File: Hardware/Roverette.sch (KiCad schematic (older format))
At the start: 40 parts, among them SW1 SW_Push, U1 ESP32-WROOM-32U

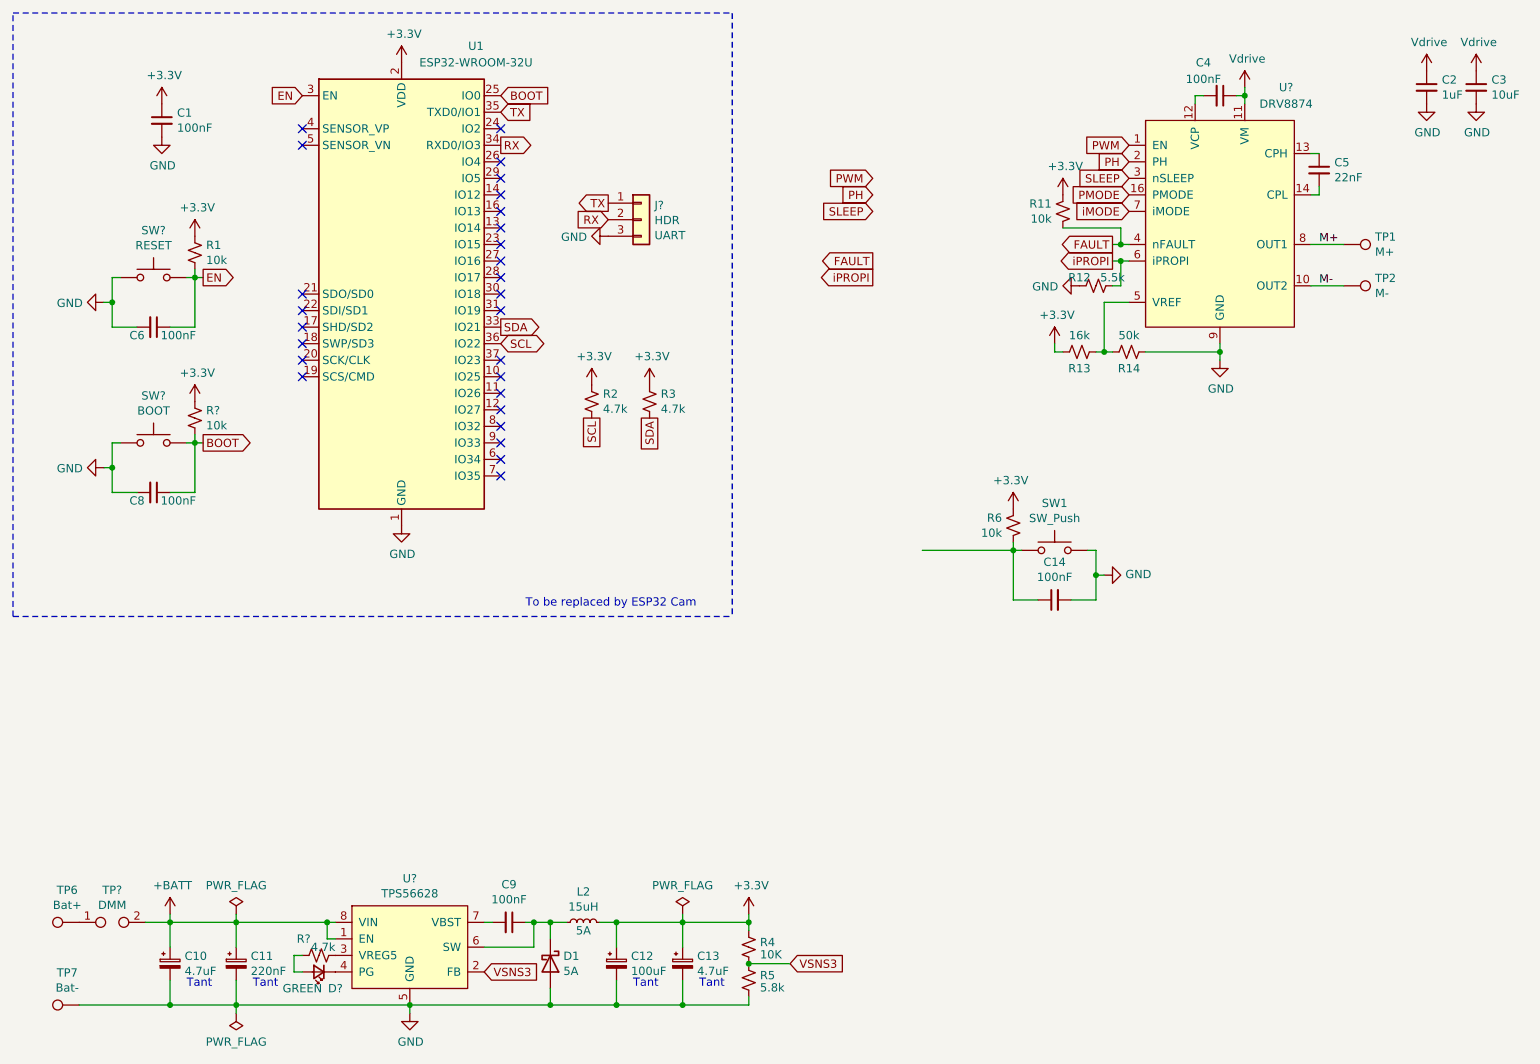
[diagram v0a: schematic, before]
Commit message: Schematic divided into sub-sheets
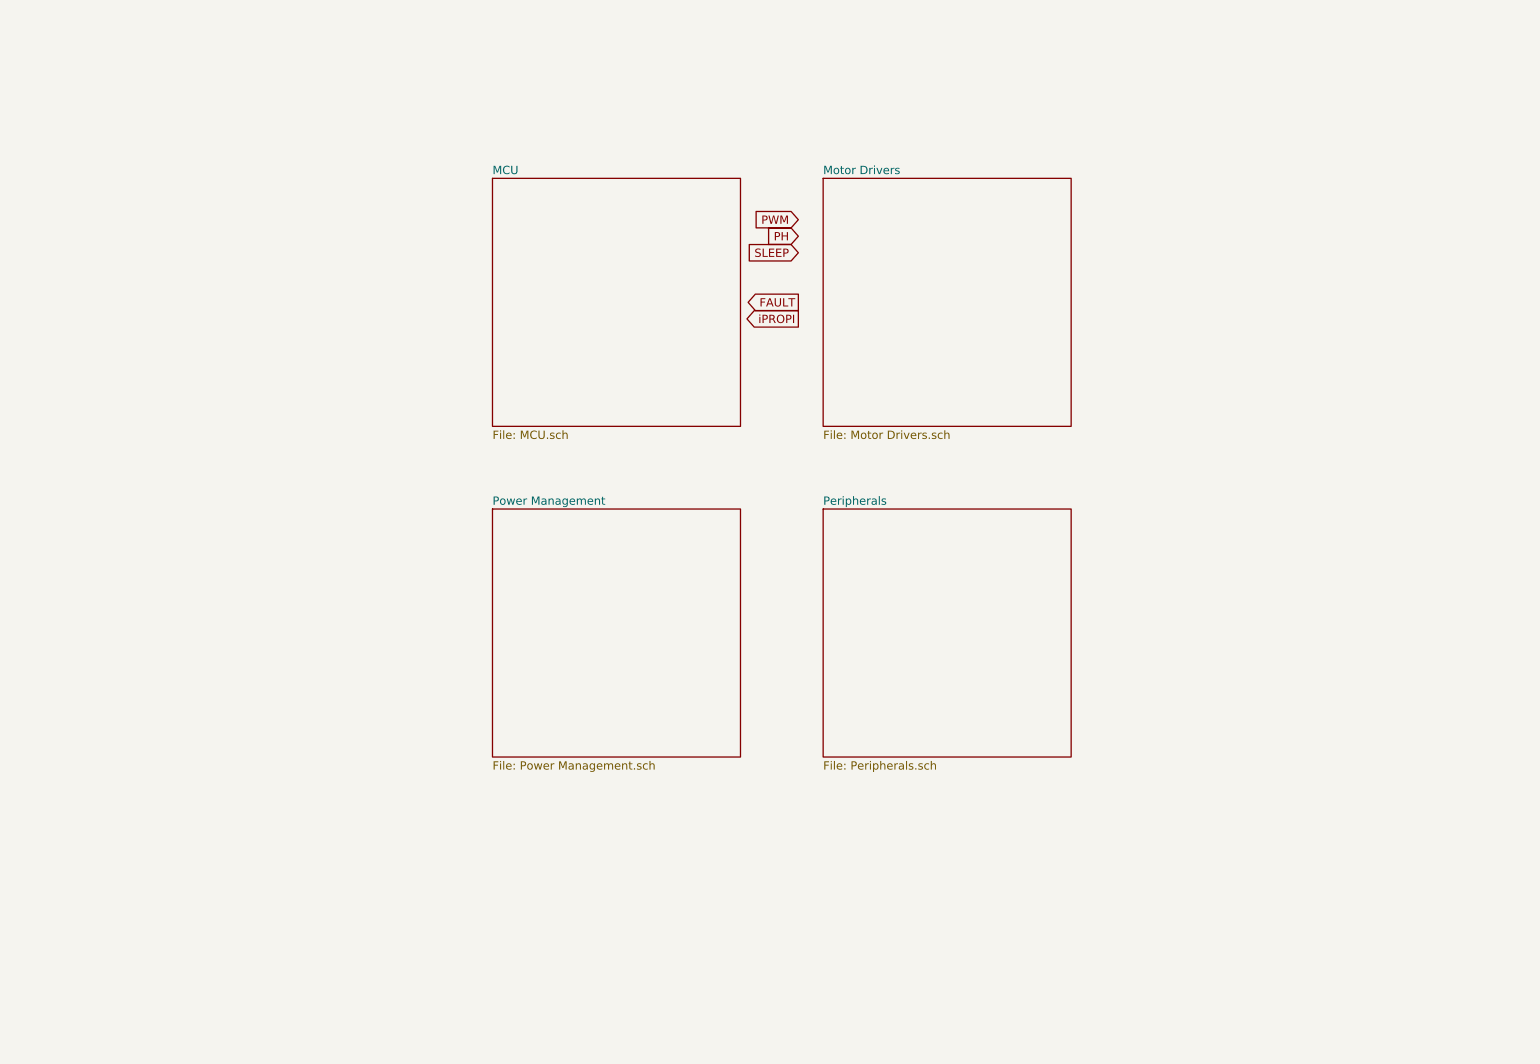
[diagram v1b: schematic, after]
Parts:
- removed C1, C14, C6, C8, C9: 100nF, Capacitor_SMD:C_0805_2012Metric, symbol Device:C_Small
- removed C10, C13: 4.7uF, Capacitor_Tantalum_SMD:CP_EIA-3528-15_AVX-H, symbol Device:CP_Small
- removed C11: 220nF, Capacitor_Tantalum_SMD:CP_EIA-3216-18_Kemet-A, symbol Device:CP_Small
- removed C12: 100uF, Capacitor_Tantalum_SMD:CP_EIA-7343-31_Kemet-D, symbol Device:CP_Small
- removed C2: 1uF, Resistor_SMD:R_0603_1608Metric, symbol Device:C_Small
- removed C3: 10uF, Capacitor_SMD:C_2220_5650Metric, symbol Device:C_Small
- removed C4: 100nF, Resistor_SMD:R_0603_1608Metric, symbol Device:C_Small
- removed C5: 22nF, Resistor_SMD:R_0603_1608Metric, symbol Device:C_Small
- removed D1: 5A, Diode_SMD:D_SOD-123F, symbol Device:D_Schottky
- removed D?: GREEN, symbol Device:LED_Small
- removed J?: HDR, symbol Connector_Generic:Conn_01x03
- removed L2: 15uH, Inductor_SMD:L_Neosid_SMs42, symbol Device:L_Small
- removed R1, R6, R?: 10k, Resistor_SMD:R_0805_2012Metric, symbol Device:R_Small_US
- removed R11: 10k, Resistor_SMD:R_0603_1608Metric, symbol Device:R_Small_US
- removed R12: 5.5k, Resistor_SMD:R_0603_1608Metric, symbol Device:R_Small_US
- removed R13: 16k, Resistor_SMD:R_0603_1608Metric, symbol Device:R_Small_US
- removed R14: 50k, Resistor_SMD:R_0603_1608Metric, symbol Device:R_Small_US
- removed R2, R3: 4.7k, Resistor_SMD:R_0603_1608Metric, symbol Device:R_Small_US
- removed R4: 10K, Resistor_SMD:R_0805_2012Metric, symbol Device:R_Small_US
- removed R5: 5.8k, Resistor_SMD:R_0805_2012Metric, symbol Device:R_Small_US
- removed R?: 4.7k, Resistor_SMD:R_0805_2012Metric, symbol Device:R_Small_US
- removed SW1, SW? (x2): SW_Push, Button_Switch_SMD:SW_SPST_CK_RS282G05A3, symbol Switch:SW_Push
- removed TP1: M+, TestPoint:TestPoint_Keystone_5000-5004_Miniature, symbol Connector:TestPoint
- removed TP2: M-, TestPoint:TestPoint_Keystone_5000-5004_Miniature, symbol Connector:TestPoint
- removed TP6: Bat+, TestPoint:TestPoint_Keystone_5000-5004_Miniature, symbol Connector:TestPoint
- removed TP7: Bat-, TestPoint:TestPoint_Keystone_5000-5004_Miniature, symbol Connector:TestPoint
- removed TP?: TestPoint_2Pole, TestPoint:TestPoint_2Pads_Pitch2.54mm_Drill0.8mm, symbol Connector:TestPoint_2Pole
- removed U1: ESP32-WROOM-32U, RF_Module:ESP32-WROOM-32U, symbol RF_Module:ESP32-WROOM-32U
- removed U?: DRV8874, Package_SO:HTSSOP-16-1EP_4.4x5mm_P0.65mm_EP3.4x5mm_Mask3x3mm_ThermalVias, symbol Driver_Motor:DRV8874
- removed U?: TPS56628, Package_SO:HSOP-8-1EP_3.9x4.9mm_P1.27mm_EP2.41x3.1mm_ThermalVias, symbol Power_Management:TPS56628
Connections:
- no-connect marks 27 -> 0
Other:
- note removed: "Tant"
- note removed: "To be replaced by ESP32 Cam"

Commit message: Motor driver and power management subsheet converted to blocks
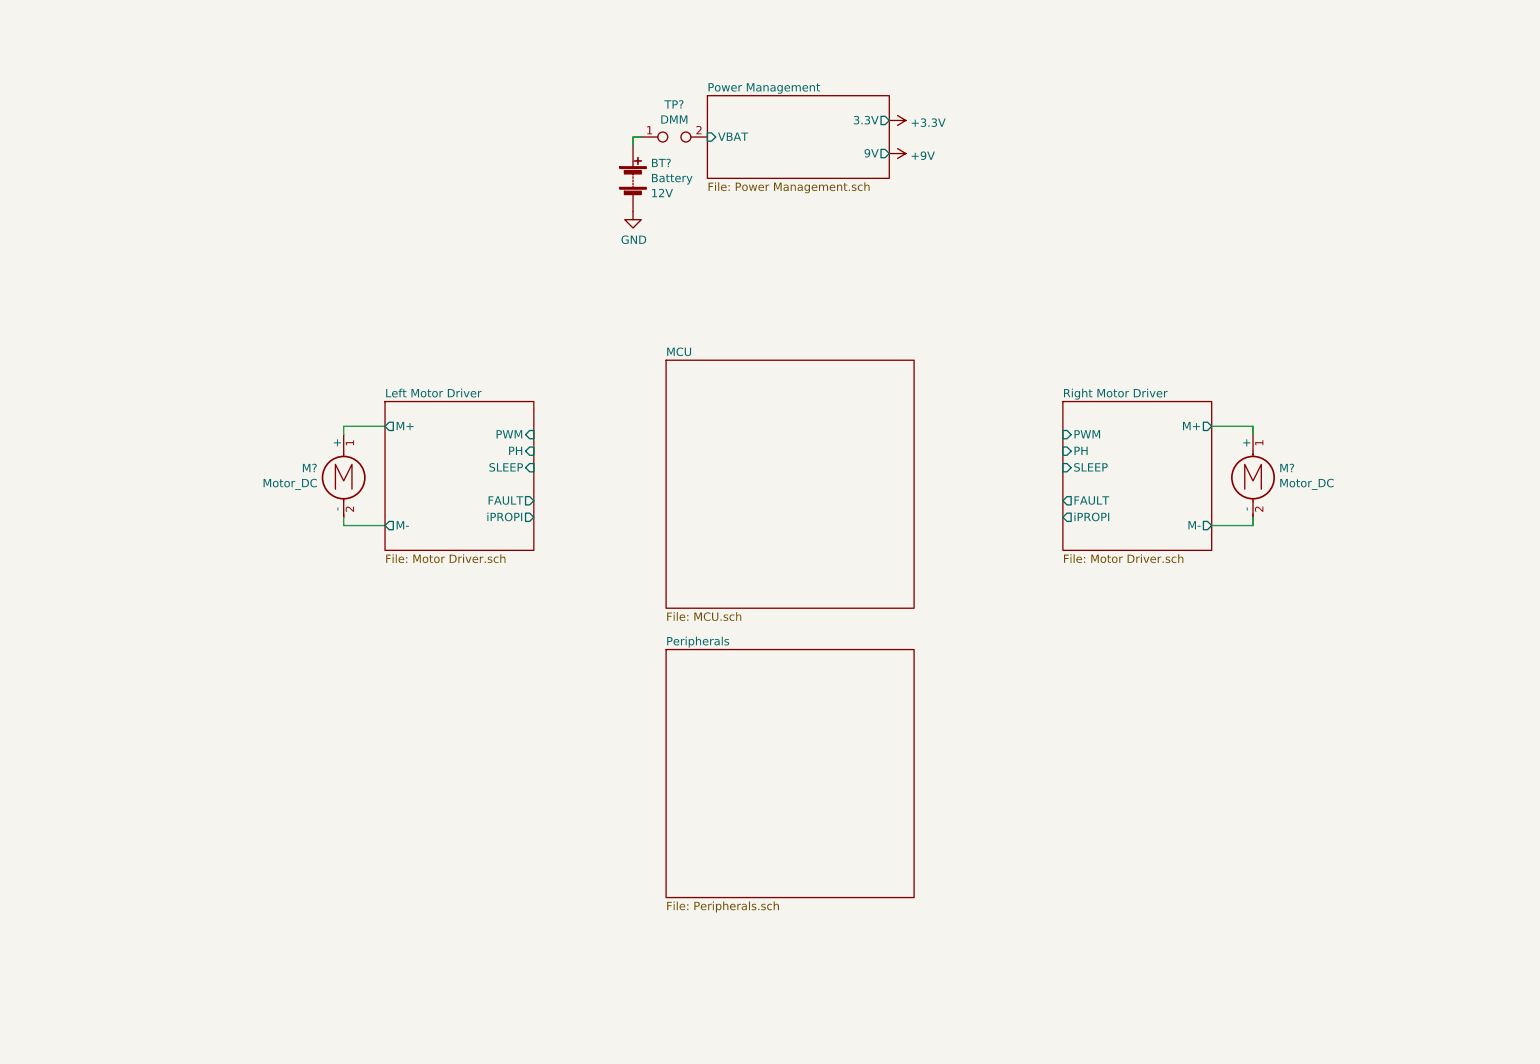
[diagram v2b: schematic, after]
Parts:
- added BT?: Battery, symbol Device:Battery
- added M? (x2): Motor_DC, symbol Motor:Motor_DC
- added TP?: TestPoint_2Pole, TestPoint:TestPoint_2Pads_Pitch2.54mm_Drill0.8mm, symbol Connector:TestPoint_2Pole
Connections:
- new net: BT?.1 (+), TP?.1
- new net GND: BT?.2 (-)
- new net Left Motor Driver/M+: M?.1 (+)
- new net Left Motor Driver/M-: M?.2 (-)
- new net Power Management/VBAT: TP?.2
- new net Right Motor Driver/M+: M?.1 (+)
- new net Right Motor Driver/M-: M?.2 (-)
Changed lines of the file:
@@
 $Descr A4 11693 8268
 encoding utf-8
-Sheet 1 5
+Sheet 1 6
 Title "Roverette"
 Date "2020-10-11"
@@
 Comment4 ""
 $EndDescr
-Text GLabel 5850 2250 0    50   Input ~ 0
-PWM
-Text GLabel 5850 2350 0    50   Input ~ 0
-PH
-Text GLabel 5850 2450 0    50   Input ~ 0
-SLEEP
-Text GLabel 5850 2750 0    50   Output ~ 0
-FAULT
-Text GLabel 5850 2850 0    50   Output ~ 0
-iPROPI
 $Sheet
-S 4000 2000 1500 1500
+S 5050 3100 1500 1500
 U 5FEFFC20
 F0 "MCU" 50
@@
 $EndSheet
 $Sheet
-S 6000 2000 1500 1500
-U 5FF00151
-F0 "Motor Drivers" 50
-F1 "Motor Drivers.sch" 50
-$EndSheet
-$Sheet
-S 4000 4000 1500 1500
+S 5300 1500 1100 500
 U 5FF0069C
 F0 "Power Management" 50
 F1 "Power Management.sch" 50
+F2 "VBAT" I L 5300 1750 50
+F3 "3.3V" O R 6400 1650 50
+F4 "9V" O R 6400 1850 50
 $EndSheet
 $Sheet
-S 6000 4000 1500 1500
+S 5050 4850 1500 1500
 U 5FF00BCF
 F0 "Peripherals" 50
 F1 "Peripherals.sch" 50
 $EndSheet
+$Sheet
+S 3350 3350 900  900
+U 5FF00151
+F0 "Left Motor Driver" 50
+F1 "Motor Driver.sch" 50
+F2 "M-" O L 3350 4100 50
+F3 "PWM" I R 4250 3550 50
+F4 "PH" I R 4250 3650 50
+F5 "SLEEP" I R 4250 3750 50
+F6 "FAULT" O R 4250 3950 50
+F7 "iPROPI" O R 4250 4050 50
+F8 "M+" O L 3350 3500 50
+$EndSheet
+$Comp
+L Motor:Motor_DC M?
+U 1 1 5FF290D9
+P 3100 3750
+F 0 "M?" H 3258 3746 50  0000 L CNN
+F 1 "Motor_DC" H 3258 3655 50  0000 L CNN
+F 2 "" H 3100 3660 50  0001 C CNN
+F 3 "~" H 3100 3660 50  0001 C CNN
+	1    3100 3750
+	-1   0    0    -1
+$EndComp
+Wire Wire Line
+	3350 3500 3100 3500
+Wire Wire Line
+	3100 3500 3100 3550
+Wire Wire Line
+	3350 4100 3100 4100
+Wire Wire Line
+	3100 4100 3100 4050
+$Sheet
+S 7450 3350 900  900
+U 5FF2CF13
+F0 "Right Motor Driver" 50
+F1 "Motor Driver.sch" 50
+F2 "M-" O R 8350 4100 50
+F3 "PWM" I L 7450 3550 50
+F4 "PH" I L 7450 3650 50
+F5 "SLEEP" I L 7450 3750 50
+F6 "FAULT" O L 7450 3950 50
+F7 "iPROPI" O L 7450 4050 50
+F8 "M+" O R 8350 3500 50
+$EndSheet
+Wire Wire Line
+	8600 4100 8600 4050
+Wire Wire Line
+	8350 4100 8600 4100
+Wire Wire Line
+	8600 3500 8600 3550
+Wire Wire Line
+	8350 3500 8600 3500
+$Comp
+L Motor:Motor_DC M?
+U 1 1 5FF2CF19
+P 8600 3750
+F 0 "M?" H 8758 3746 50  0000 L CNN
+F 1 "Motor_DC" H 8758 3655 50  0000 L CNN
+F 2 "" H 8600 3660 50  0001 C CNN
+F 3 "~" H 8600 3660 50  0001 C CNN
+	1    8600 3750
+	1    0    0    -1
+$EndComp
+$Comp
+L power:+3.3V #PWR?
+U 1 1 5FF308D0
+P 6400 1650
+F 0 "#PWR?" H 6400 1500 50  0001 C CNN
+F 1 "+3.3V" V 6415 1778 50  0000 L CNN
+F 2 "" H 6400 1650 50  0001 C CNN
+F 3 "" H 6400 1650 50  0001 C CNN
+	1    6400 1650
+	0    1    1    0
+$EndComp
+$Comp
+L power:+9V #PWR?
+U 1 1 5FF30D7D
+P 6400 1850
+F 0 "#PWR?" H 6400 1700 50  0001 C CNN
+F 1 "+9V" V 6415 1978 50  0000 L CNN
+F 2 "" H 6400 1850 50  0001 C CNN
+F 3 "" H 6400 1850 50  0001 C CNN
+	1    6400 1850
+	0    1    1    0
+$EndComp
+$Comp
+L Device:Battery BT?
+U 1 1 5FF30336
+P 4850 2000
+F 0 "BT?" H 4958 2091 50  0000 L CNN
+F 1 "Battery" H 4958 2000 50  0000 L CNN
+F 2 "" V 4850 2060 50  0001 C CNN
+F 3 "~" V 4850 2060 50  0001 C CNN
+F 4 "12V" H 4958 1909 50  0000 L CNN "Field4"
+	1    4850 2000
+	1    0    0    -1
+$EndComp
+$Comp
+L power:GND #PWR?
+U 1 1 5FF31DAB
+P 4850 2200
+F 0 "#PWR?" H 4850 1950 50  0001 C CNN
+F 1 "GND" H 4855 2027 50  0000 C CNN
+F 2 "" H 4850 2200 50  0001 C CNN
+F 3 "" H 4850 2200 50  0001 C CNN
+	1    4850 2200
+	1    0    0    -1
+$EndComp
+$Comp
+L Connector:TestPoint_2Pole TP?
+U 1 1 5FF3E3D0
+P 5100 1750
+AR Path="/5FF3E3D0" Ref="TP?"  Part="1"
+AR Path="/5FF0069C/5FF3E3D0" Ref="TP?"  Part="1"
+F 0 "TP?" H 5100 1945 50  0000 C CNN
+F 1 "TestPoint_2Pole" H 5100 1854 50  0001 C CNN
+F 2 "TestPoint:TestPoint_2Pads_Pitch2.54mm_Drill0.8mm" H 5100 1750 50  0001 C CNN
+F 3 "~" H 5100 1750 50  0001 C CNN
+F 4 "DMM" H 5100 1854 50  0000 C CNN "Field4"
+	1    5100 1750
+	1    0    0    -1
+$EndComp
+Wire Wire Line
+	4900 1750 4850 1750
+Wire Wire Line
+	4850 1750 4850 1800
 $EndSCHEMATC

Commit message: Readme updated
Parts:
- gave numbers to parts that had none: 4
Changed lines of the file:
@@
 $EndSheet
 $Comp
-L Motor:Motor_DC M?
+L Motor:Motor_DC M1
 U 1 1 5FF290D9
 P 3100 3750
-F 0 "M?" H 3258 3746 50  0000 L CNN
+F 0 "M1" H 3258 3746 50  0000 L CNN
 F 1 "Motor_DC" H 3258 3655 50  0000 L CNN
 F 2 "" H 3100 3660 50  0001 C CNN
@@
 	8350 3500 8600 3500
 $Comp
-L Motor:Motor_DC M?
+L Motor:Motor_DC M2
 U 1 1 5FF2CF19
 P 8600 3750
-F 0 "M?" H 8758 3746 50  0000 L CNN
+F 0 "M2" H 8758 3746 50  0000 L CNN
 F 1 "Motor_DC" H 8758 3655 50  0000 L CNN
 F 2 "" H 8600 3660 50  0001 C CNN
@@
 $EndComp
 $Comp
-L power:+3.3V #PWR?
+L power:+3.3V #PWR01
 U 1 1 5FF308D0
 P 6400 1650
-F 0 "#PWR?" H 6400 1500 50  0001 C CNN
+F 0 "#PWR01" H 6400 1500 50  0001 C CNN
 F 1 "+3.3V" V 6415 1778 50  0000 L CNN
 F 2 "" H 6400 1650 50  0001 C CNN
@@
 $EndComp
 $Comp
-L power:+9V #PWR?
+L power:+9V #PWR02
 U 1 1 5FF30D7D
 P 6400 1850
-F 0 "#PWR?" H 6400 1700 50  0001 C CNN
+F 0 "#PWR02" H 6400 1700 50  0001 C CNN
 F 1 "+9V" V 6415 1978 50  0000 L CNN
 F 2 "" H 6400 1850 50  0001 C CNN
@@
 $EndComp
 $Comp
-L Device:Battery BT?
+L Device:Battery BT1
 U 1 1 5FF30336
 P 4850 2000
-F 0 "BT?" H 4958 2091 50  0000 L CNN
+F 0 "BT1" H 4958 2091 50  0000 L CNN
 F 1 "Battery" H 4958 2000 50  0000 L CNN
 F 2 "" V 4850 2060 50  0001 C CNN
@@
 $EndComp
 $Comp
-L power:GND #PWR?
+L power:GND #PWR03
 U 1 1 5FF31DAB
 P 4850 2200
-F 0 "#PWR?" H 4850 1950 50  0001 C CNN
+F 0 "#PWR03" H 4850 1950 50  0001 C CNN
 F 1 "GND" H 4855 2027 50  0000 C CNN
 F 2 "" H 4850 2200 50  0001 C CNN
@@
 $EndComp
 $Comp
-L Connector:TestPoint_2Pole TP?
+L Connector:TestPoint_2Pole TP1
 U 1 1 5FF3E3D0
 P 5100 1750
-AR Path="/5FF3E3D0" Ref="TP?"  Part="1"
+AR Path="/5FF3E3D0" Ref="TP1"  Part="1"
 AR Path="/5FF0069C/5FF3E3D0" Ref="TP?"  Part="1"
-F 0 "TP?" H 5100 1945 50  0000 C CNN
+F 0 "TP1" H 5100 1945 50  0000 C CNN
 F 1 "TestPoint_2Pole" H 5100 1854 50  0001 C CNN
 F 2 "TestPoint:TestPoint_2Pads_Pitch2.54mm_Drill0.8mm" H 5100 1750 50  0001 C CNN

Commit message: Signed-off-by: Usman Mehmood <usmanmehmood55@gmail.com>
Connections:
- net Charger/BATT: now reaches BT1.1 (+), TP1.1
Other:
- moved on the sheet: BT1, M1, M2, TP1

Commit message: Schematic and readme updated
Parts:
- TP1: symbol Connector:TestPoint_2Pole -> Device:Jumper
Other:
- moved on the sheet: BT1
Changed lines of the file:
@@
 $EndComp
 Wire Wire Line
-	4450 2300 4450 2350
+	4350 2300 4350 2350
 $Comp
-L Connector:TestPoint_2Pole TP1
+L Device:Jumper TP1
 U 1 1 5FF3E3D0
-P 4800 2300
+P 4700 2300
 AR Path="/5FF3E3D0" Ref="TP1"  Part="1"
 AR Path="/5FF0069C/5FF3E3D0" Ref="TP?"  Part="1"
-F 0 "TP1" H 4800 2495 50  0000 C CNN
-F 1 "TestPoint_2Pole" H 4800 2404 50  0001 C CNN
-F 2 "TestPoint:TestPoint_2Pads_Pitch2.54mm_Drill0.8mm" H 4800 2300 50  0001 C CNN
-F 3 "~" H 4800 2300 50  0001 C CNN
-F 4 "DMM" H 4800 2404 50  0000 C CNN "Field4"
-	1    4800 2300
+F 0 "TP1" H 4700 2550 50  0000 C CNN
+F 1 "TestPoint_2Pole" H 4700 2404 50  0001 C CNN
+F 2 "TestPoint:TestPoint_2Pads_Pitch2.54mm_Drill0.8mm" H 4700 2300 50  0001 C CNN
+F 3 "~" H 4700 2300 50  0001 C CNN
+F 4 "DMM" H 4700 2450 50  0000 C CNN "Field4"
+	1    4700 2300
 	1    0    0    -1
 $EndComp
@@
 L power:GND #PWR03
 U 1 1 5FF31DAB
-P 4450 2750
-F 0 "#PWR03" H 4450 2500 50  0001 C CNN
-F 1 "GND" H 4455 2577 50  0000 C CNN
-F 2 "" H 4450 2750 50  0001 C CNN
-F 3 "" H 4450 2750 50  0001 C CNN
-	1    4450 2750
+P 4350 2750
+F 0 "#PWR03" H 4350 2500 50  0001 C CNN
+F 1 "GND" H 4355 2577 50  0000 C CNN
+F 2 "" H 4350 2750 50  0001 C CNN
+F 3 "" H 4350 2750 50  0001 C CNN
+	1    4350 2750
 	1    0    0    -1
 $EndComp
@@
 L Device:Battery BT1
 U 1 1 5FF30336
-P 4450 2550
-F 0 "BT1" H 4558 2641 50  0000 L CNN
-F 1 "Battery" H 4558 2550 50  0000 L CNN
-F 2 "" V 4450 2610 50  0001 C CNN
-F 3 "~" V 4450 2610 50  0001 C CNN
-F 4 "12V" H 4558 2459 50  0000 L CNN "Field4"
-	1    4450 2550
+P 4350 2550
+F 0 "BT1" H 4458 2641 50  0000 L CNN
+F 1 "Battery" H 4458 2550 50  0000 L CNN
+F 2 "" V 4350 2610 50  0001 C CNN
+F 3 "~" V 4350 2610 50  0001 C CNN
+F 4 "12V" H 4458 2459 50  0000 L CNN "Field4"
+	1    4350 2550
 	1    0    0    -1
 $EndComp
@@
 Wire Wire Line
 	6350 3350 6100 3350
-Connection ~ 4450 2300
-Wire Wire Line
-	4450 2300 3900 2300
-Wire Wire Line
-	4450 2300 4600 2300
 $Sheet
 S 5000 2050 1100 500
@@
 F4 "9V" O R 6100 2400 50
 $EndSheet
+Wire Wire Line
+	4350 2300 3900 2300
+Wire Wire Line
+	4400 2300 4350 2300
+Connection ~ 4350 2300
 $EndSCHEMATC

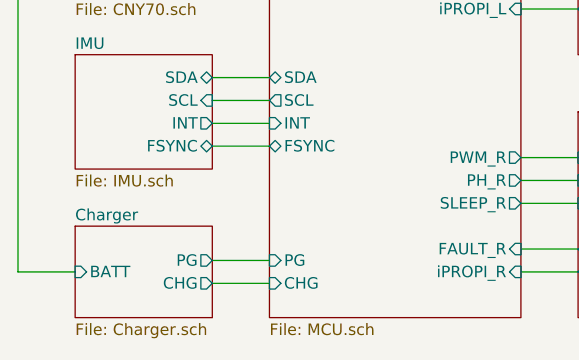
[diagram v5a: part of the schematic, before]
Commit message: Battery charger IC added
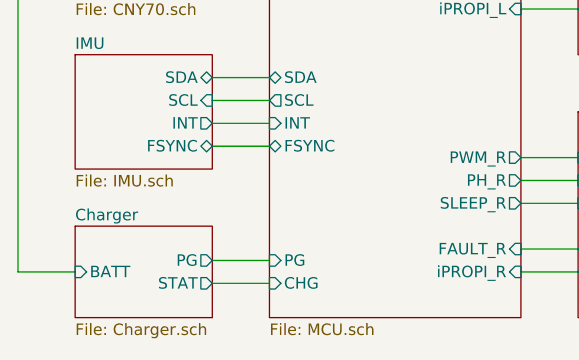
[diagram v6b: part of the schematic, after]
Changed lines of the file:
@@
 F1 "Charger.sch" 50
 F2 "PG" O R 4750 4950 50
-F3 "CHG" O R 4750 5050 50
-F4 "BATT" I L 4150 5000 50
+F3 "BATT" I L 4150 5000 50
+F4 "STAT" O R 4750 5050 50
 $EndSheet
 Wire Wire Line
